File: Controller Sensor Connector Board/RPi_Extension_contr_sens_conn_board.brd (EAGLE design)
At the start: 100 x 100 mm, 51 parts, among them J1 22-27-2051-05, J2 22-27-2051-05, U1 5103309-7, X17 53047-03, X18 53047-03, X19 53047-03, X20 53047-03, X21 53047-03, X22 53047-03, X23 53047-03, X24 53047-03, X25 53047-03, X26 53047-03, X27 53047-03, X28 53047-03, X29 53047-03, X30 53047-03, X31 53047-03, X32 53047-03

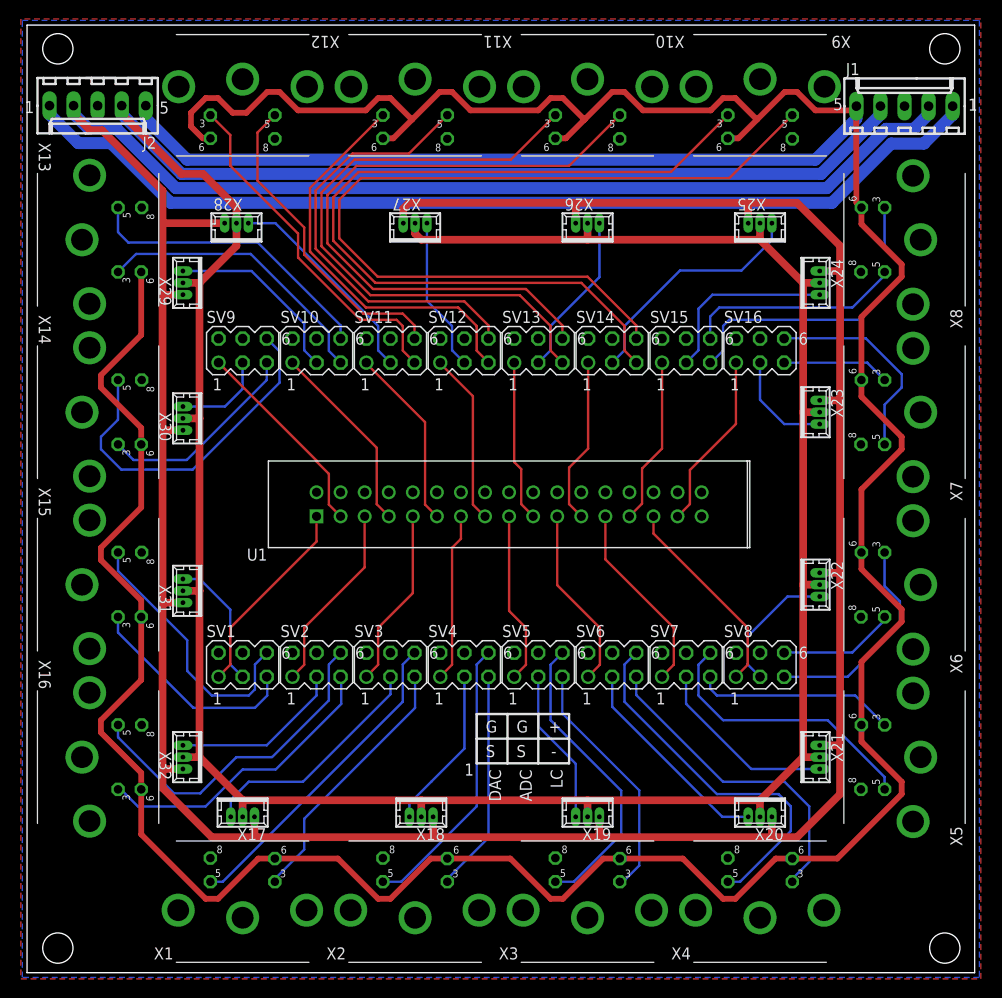
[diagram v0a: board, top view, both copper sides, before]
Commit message: using jst-ph connectors instead of molex micro blade
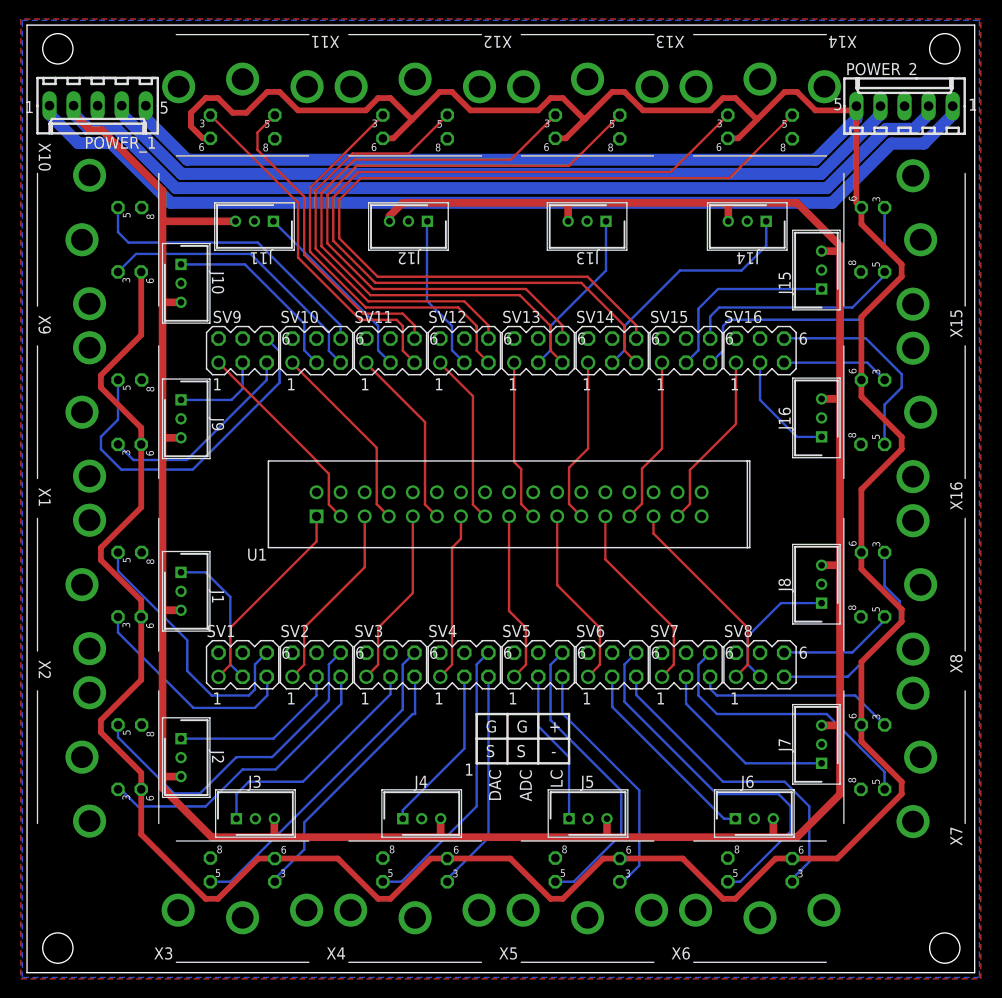
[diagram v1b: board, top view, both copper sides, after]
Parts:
- removed X17, X18, X19, X20, X21, X22, X23, X24, X25, X26, X27, X28, X29, X30, X31, X32: 53047-03, con-molex:53047-03
- added J10, J11, J12, J13, J14, J15, J16, J3, J4, J5, J6, J7, J8, J9: B3B-PH-K-S(LF)(SN), JST_PH:SHDR3W50P0X200_1X3_790X450X600
- added POWER_1, POWER_2: 22-27-2051-05, con-molex:6410-05
- J1, J2: value 22-27-2051-05 -> B3B-PH-K-S(LF)(SN); device con-molex:6410-05 -> JST_PH:SHDR3W50P0X200_1X3_790X450X600
- moved X15 95.6 mm to (94.2, 77.3), turned to 270 degrees
- moved X16 95.6 mm to (94.2, 59.1), turned to 270 degrees
- moved J1 90.8 mm to (16.2, 42.2), turned to 270 degrees
- moved X14 79.7 mm to (77.3, 94.2), turned to 0 degrees
- moved X9 79.7 mm to (5.85, 59.1), turned to 90 degrees
- moved J2 67.4 mm to (16.2, 24.7), turned to 270 degrees
- moved X10 55.9 mm to (5.85, 77.3), turned to 90 degrees
- moved X13 55.9 mm to (59.1, 94.2), turned to 0 degrees
- moved X6 39.0 mm to (77.3, 5.85), turned to 180 degrees
- moved X1 39.0 mm to (5.85, 41.0), turned to 90 degrees
- moved X2 39.0 mm to (5.85, 22.8), turned to 90 degrees
- moved X5 39.0 mm to (59.1, 5.85), turned to 180 degrees
- moved X3 36.4 mm to (22.8, 5.85)
- moved X7 36.4 mm to (94.2, 22.8)
- moved X4 36.4 mm to (41.0, 5.85)
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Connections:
- net +12V: now also J1.3, J10.3, J11.3, J12.3, J13.3, J14.3, J15.3, J16.3, J2.3, J3.3, J4.3, J5.3, J6.3, J7.3, J8.3, J9.3, POWER_1.2, POWER_2.2; no longer J1.2, J2.2, X17.3, X18.3, X19.3, X20.3, X21.3, X22.3, X23.3, X24.3, X25.3, X26.3, X27.3, X28.3, X29.3, X30.3, X31.3, X32.3
- net +3_3V: now also POWER_1.1, POWER_2.1; no longer J1.1, J2.1
- net +5V: now also POWER_1.5, POWER_2.5; no longer J1.5, J2.5
- net -12V: now also POWER_1.4, POWER_2.4; no longer J1.4, J2.4, X17.2, X18.2, X19.2, X20.2, X21.2, X22.2, X23.2, X24.2, X25.2, X26.2, X27.2, X28.2, X29.2, X30.2, X31.2, X32.2
- net ADC_1: now also J1.1; no longer X31.1
- net ADC_10: now also J10.1; no longer X29.1
- net ADC_11: now also J11.1; no longer X28.1
- net ADC_12: now also J12.1; no longer X27.1
- net ADC_13: now also J13.1; no longer X26.1
- net ADC_14: now also J14.1; no longer X25.1
- net ADC_15: now also J15.1; no longer X24.1
- net ADC_16: now also J16.1; no longer X23.1
- net ADC_2: now also J2.1; no longer X32.1
- net ADC_3: now also J3.1; no longer X17.1
- net ADC_4: now also J4.1; no longer X18.1
- net ADC_5: now also J5.1; no longer X19.1
- net ADC_6: now also J6.1; no longer X20.1
- net ADC_7: now also J7.1; no longer X21.1
- net ADC_8: now also J8.1; no longer X22.1
- net ADC_9: now also J9.1; no longer X30.1
- net GND: now also J1.2, J10.2, J11.2, J12.2, J13.2, J14.2, J15.2, J16.2, J2.2, J3.2, J4.2, J5.2, J6.2, J7.2, J8.2, J9.2, POWER_1.3, POWER_2.3; no longer J1.3, J2.3
- net LC_N_1: now also X1.3; no longer X15.3
- net LC_N_10: now also X10.3; no longer X13.3
- net LC_N_11: now also X11.3; no longer X12.3
- net LC_N_12: now also X12.3; no longer X11.3
- net LC_N_13: now also X13.3; no longer X10.3
- net LC_N_14: now also X14.3; no longer X9.3
- net LC_N_15: now also X15.3; no longer X8.3
- net LC_N_16: now also X16.3; no longer X7.3
- net LC_N_2: now also X2.3; no longer X16.3
- net LC_N_3: now also X3.3; no longer X1.3
- net LC_N_4: now also X4.3; no longer X2.3
- net LC_N_5: now also X5.3; no longer X3.3
- net LC_N_6: now also X6.3; no longer X4.3
- net LC_N_7: now also X7.3; no longer X5.3
- net LC_N_8: now also X8.3; no longer X6.3
- net LC_N_9: now also X9.3; no longer X14.3
- net LC_P_1: now also X1.5; no longer X15.5
- net LC_P_10: now also X10.5; no longer X13.5
- net LC_P_11: now also X11.5; no longer X12.5
- net LC_P_12: now also X12.5; no longer X11.5
- net LC_P_13: now also X13.5; no longer X10.5
- net LC_P_14: now also X14.5; no longer X9.5
- net LC_P_15: now also X15.5; no longer X8.5
- net LC_P_16: now also X16.5; no longer X7.5
- net LC_P_2: now also X2.5; no longer X16.5
- net LC_P_3: now also X3.5; no longer X1.5
- net LC_P_4: now also X4.5; no longer X2.5
- net LC_P_5: now also X5.5; no longer X3.5
- net LC_P_6: now also X6.5; no longer X4.5
- net LC_P_7: now also X7.5; no longer X5.5
- net LC_P_8: now also X8.5; no longer X6.5
- net LC_P_9: now also X9.5; no longer X14.5
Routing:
- net -12V: track 350.0 -> 87.9 mm
- net ADC_11: track 22.6 -> 20.0 mm
- net ADC_6: track 22.3 -> 21.1 mm
- net ADC_1: track 14.0 -> 15.2 mm
- net ADC_16: track 11.3 -> 12.0 mm
- net +12V: track 395.3 -> 394.6 mm

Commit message: disconnected shorting ground connection on connector board
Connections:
- net GND: no longer U1.34
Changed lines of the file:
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@@
 <contactref element="SV12" pad="4"/>
 <contactref element="SV16" pad="4"/>
-<contactref element="U1" pad="34"/>
 <contactref element="U1" pad="2"/>
 <contactref element="U1" pad="4"/>
